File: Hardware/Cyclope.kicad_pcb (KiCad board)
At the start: 2 copper layers, 100 x 84 mm, 81 parts, among them J1 M20-9762042, J2 Motor_2, J3 Motor_1, J4 Front, J5 Front, J8 FTDI, M1 FS5113R, M2 FS5113R, Q1 DMG3414U, Q2 DMG2301L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

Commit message: (Hardware] Renamed motherboard PCB mounting holes for more coherency.
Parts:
- H10, H7, H8, H9: value Raspberry_Pi -> Motherboard
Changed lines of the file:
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@@
       (effects (font (size 1 1) (thickness 0.15)))
     )
-    (fp_text value Raspberry_Pi (at 0 4.2) (layer F.Fab) hide
+    (fp_text value Motherboard (at 0 4.2) (layer F.Fab) hide
       (effects (font (size 1 1) (thickness 0.15)))
     )
@@
       (effects (font (size 1 1) (thickness 0.15)))
     )
-    (fp_text value Raspberry_Pi (at 0 4.2) (layer F.Fab) hide
+    (fp_text value Motherboard (at 0 4.2) (layer F.Fab) hide
       (effects (font (size 1 1) (thickness 0.15)))
     )
@@
       (effects (font (size 1 1) (thickness 0.15)))
     )
-    (fp_text value Raspberry_Pi (at 0 4.2) (layer F.Fab) hide
+    (fp_text value Motherboard (at 0 4.2) (layer F.Fab) hide
       (effects (font (size 1 1) (thickness 0.15)))
     )
@@
       (effects (font (size 1 1) (thickness 0.15)))
     )
-    (fp_text value Raspberry_Pi (at 0 4.2) (layer F.Fab) hide
+    (fp_text value Motherboard (at 0 4.2) (layer F.Fab) hide
       (effects (font (size 1 1) (thickness 0.15)))
     )

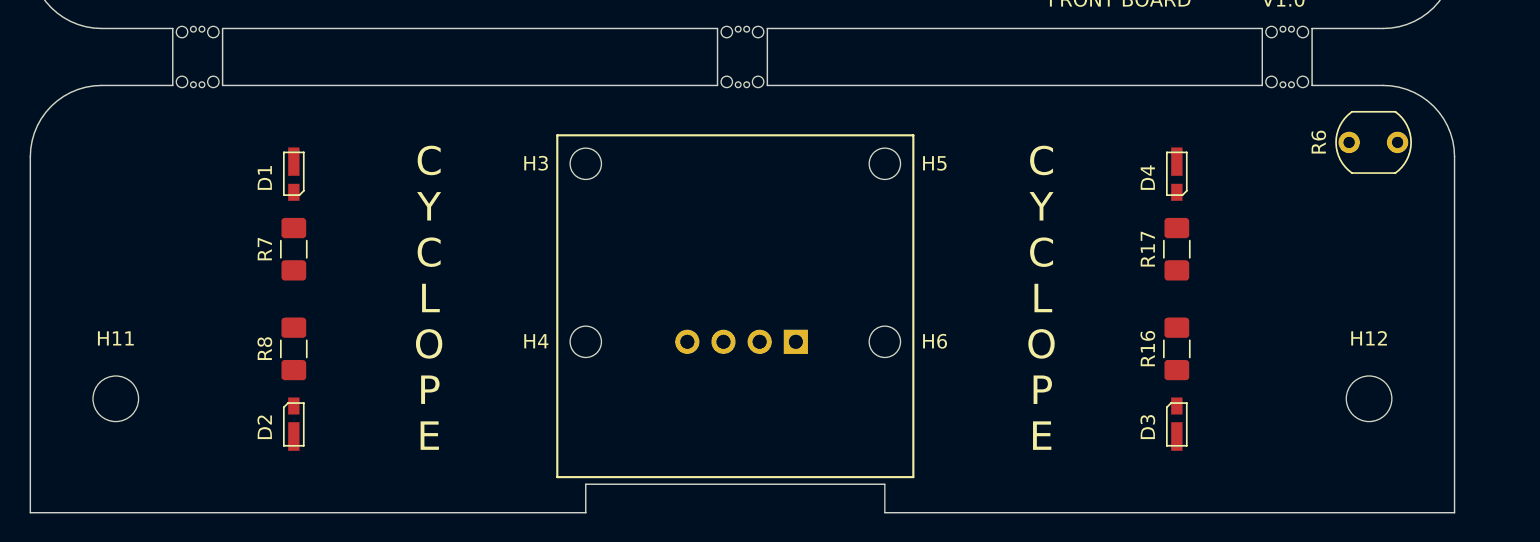
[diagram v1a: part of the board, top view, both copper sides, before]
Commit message: [Hardware] Routed front board PCB.
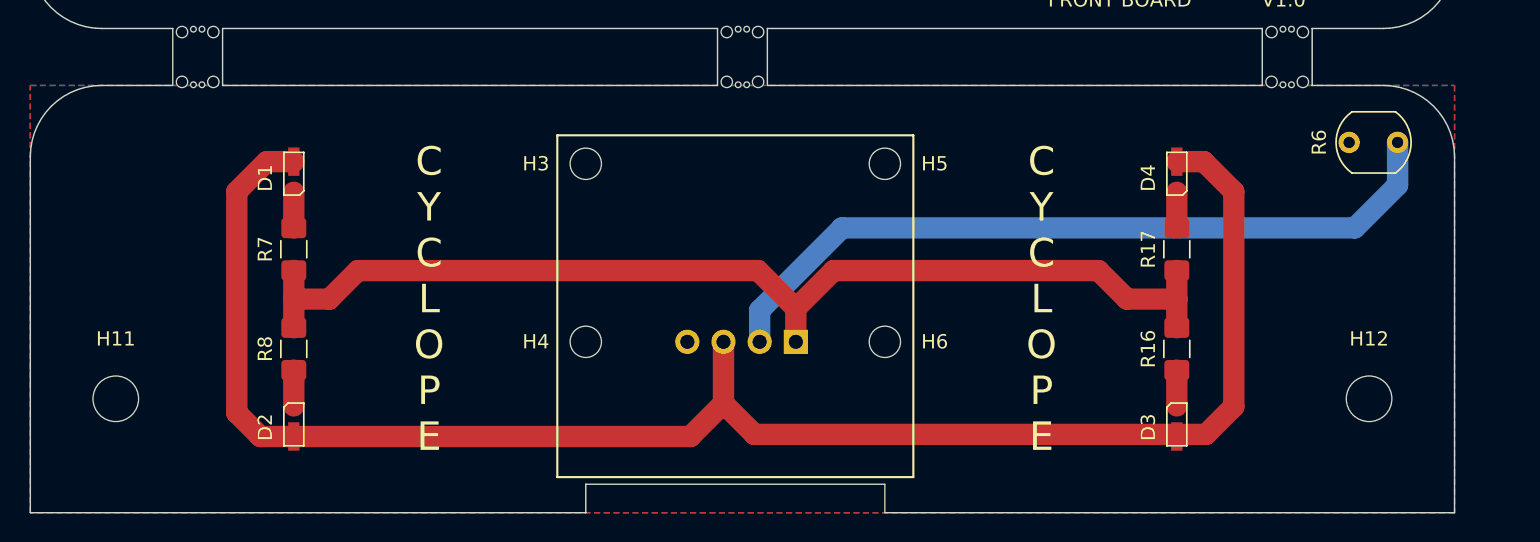
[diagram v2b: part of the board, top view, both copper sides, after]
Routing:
- net Net-(D1-Pad1): track 0.00 -> 118.1 mm
- net +5VD: track 0.00 -> 76.3 mm
- net Net-(J4-Pad2): track 0.00 -> 53.6 mm
- net Net-(D4-Pad2): track 0.00 -> 2.51 mm
- net Net-(D1-Pad2): track 0.00 -> 2.51 mm
- net Net-(D3-Pad2): track 0.00 -> 2.51 mm
- net Net-(D2-Pad2): track 0.00 -> 2.51 mm
- added copper zone on B.Cu, net GNDD
- added copper zone on F.Cu, net GNDD
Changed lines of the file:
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@@
     (thickness 1.6)
     (drawings 64)
-    (tracks 0)
+    (tracks 36)
     (zones 0)
     (modules 81)
@@
   )
   (setup
-    (last_trace_width 0.25)
+    (last_trace_width 1.5)
+    (user_trace_width 1.5)
     (trace_clearance 0.2)
-    (zone_clearance 0.508)
+    (zone_clearance 0.127)
     (zone_45_only no)
     (trace_min 0.2)
@@
     (effects (font (size 1 1) (thickness 0.15)))
   )
+  (segment (start 74.1 119.35) (end 72 121.45) (width 1.5) (layer F.Cu) (net 42))
+  (segment (start 76 119.35) (end 74.1 119.35) (width 1.5) (layer F.Cu) (net 42))
+  (segment (start 72 121.45) (end 72 137) (width 1.5) (layer F.Cu) (net 42))
+  (segment (start 73.65 138.65) (end 76 138.65) (width 1.5) (layer F.Cu) (net 42))
+  (segment (start 72 137) (end 73.65 138.65) (width 1.5) (layer F.Cu) (net 42))
+  (segment (start 76 138.65) (end 103.85 138.65) (width 1.5) (layer F.Cu) (net 42))
+  (segment (start 106.17 136.33) (end 106.17 132) (width 1.5) (layer F.Cu) (net 42))
+  (segment (start 103.85 138.65) (end 106.17 136.33) (width 1.5) (layer F.Cu) (net 42))
+  (segment (start 139.9 119.35) (end 142 121.45) (width 1.5) (layer F.Cu) (net 42))
+  (segment (start 138 119.35) (end 139.9 119.35) (width 1.5) (layer F.Cu) (net 42))
+  (segment (start 142 136.55) (end 140.05 138.5) (width 1.5) (layer F.Cu) (net 42))
+  (segment (start 142 121.45) (end 142 136.55) (width 1.5) (layer F.Cu) (net 42))
+  (segment (start 108.34 138.5) (end 106.17 136.33) (width 1.5) (layer F.Cu) (net 42))
+  (segment (start 140.05 138.5) (end 108.34 138.5) (width 1.5) (layer F.Cu) (net 42))
+  (segment (start 76 121.5) (end 76 124.0125) (width 1.5) (layer F.Cu) (net 43))
+  (segment (start 76 133.9875) (end 76 136.5) (width 1.5) (layer F.Cu) (net 44))
+  (segment (start 111.25 129.65) (end 113.9 127) (width 1.5) (layer F.Cu) (net 46))
+  (segment (start 111.25 132) (end 111.25 129.65) (width 1.5) (layer F.Cu) (net 46))
+  (segment (start 113.9 127) (end 132.5 127) (width 1.5) (layer F.Cu) (net 46))
+  (segment (start 138 129) (end 134.5 129) (width 1.5) (layer F.Cu) (net 46))
+  (segment (start 134.5 129) (end 132.5 127) (width 1.5) (layer F.Cu) (net 46))
+  (segment (start 138 126.9875) (end 138 129) (width 1.5) (layer F.Cu) (net 46))
+  (segment (start 138 129) (end 138 131.0125) (width 1.5) (layer F.Cu) (net 46))
+  (segment (start 76 126.9875) (end 76 129) (width 1.5) (layer F.Cu) (net 46))
+  (segment (start 76 129) (end 76 131.0125) (width 1.5) (layer F.Cu) (net 46))
+  (segment (start 108.6 127) (end 111.25 129.65) (width 1.5) (layer F.Cu) (net 46))
+  (segment (start 80.5 127) (end 108.6 127) (width 1.5) (layer F.Cu) (net 46))
+  (segment (start 78.5 129) (end 80.5 127) (width 1.5) (layer F.Cu) (net 46))
+  (segment (start 76 129) (end 78.5 129) (width 1.5) (layer F.Cu) (net 46))
+  (segment (start 138 133.9875) (end 138 136.5) (width 1.5) (layer F.Cu) (net 56))
+  (segment (start 138 121.5) (end 138 124.0125) (width 1.5) (layer F.Cu) (net 57))
+  (segment (start 153.5 121) (end 153.5 118) (width 1.5) (layer B.Cu) (net 59))
+  (segment (start 114.5 124) (end 150.5 124) (width 1.5) (layer B.Cu) (net 59))
+  (segment (start 108.71 129.79) (end 114.5 124) (width 1.5) (layer B.Cu) (net 59))
+  (segment (start 150.5 124) (end 153.5 121) (width 1.5) (layer B.Cu) (net 59))
+  (segment (start 108.71 132) (end 108.71 129.79) (width 1.5) (layer B.Cu) (net 59))
   (zone (net 0) (net_name "") (layers F&B.Cu) (hatch edge 0.508)
     (connect_pads (clearance 0.508))
@@
       )
     )
+  )
+  (zone (net 45) (net_name GNDD) (layer F.Cu) (hatch edge 0.508)
+    (connect_pads (clearance 0.127))
+    (min_thickness 0.254)
+    (fill yes (arc_segments 32) (thermal_gap 0.508) (thermal_bridge_width 0.508))
+    (polygon
+      (pts
+        (xy 157.5 144) (xy 57.5 144) (xy 57.5 114) (xy 157.5 114)
+      )
+    )
+  )
+  (zone (net 45) (net_name GNDD) (layer B.Cu) (hatch edge 0.508)
+    (connect_pads (clearance 0.127))
+    (min_thickness 0.254)
+    (fill yes (arc_segments 32) (thermal_gap 0.508) (thermal_bridge_width 0.508))
+    (polygon
+      (pts
+        (xy 157.5 144) (xy 57.5 144) (xy 57.5 114) (xy 157.5 114)
+      )
+    )

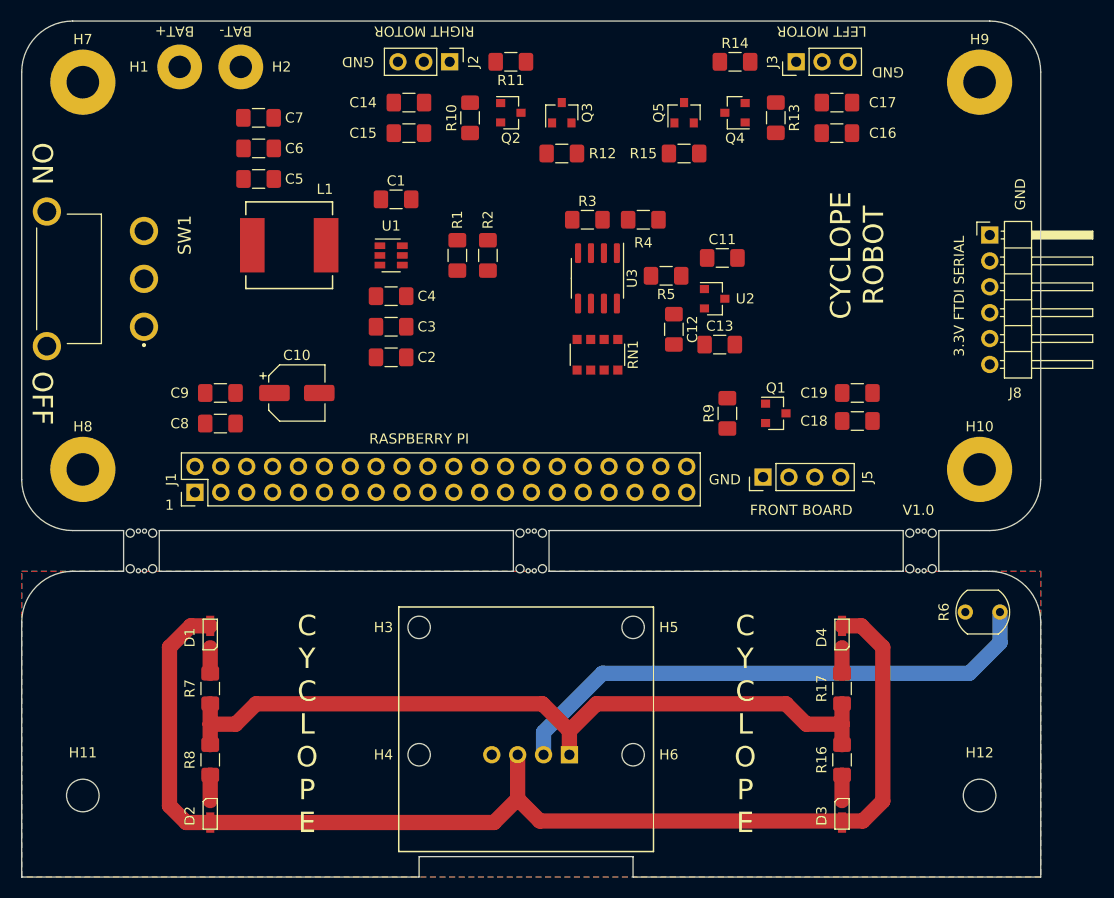
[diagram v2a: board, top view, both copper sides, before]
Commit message: [Hardware] Routed motherboard left motor transistors.
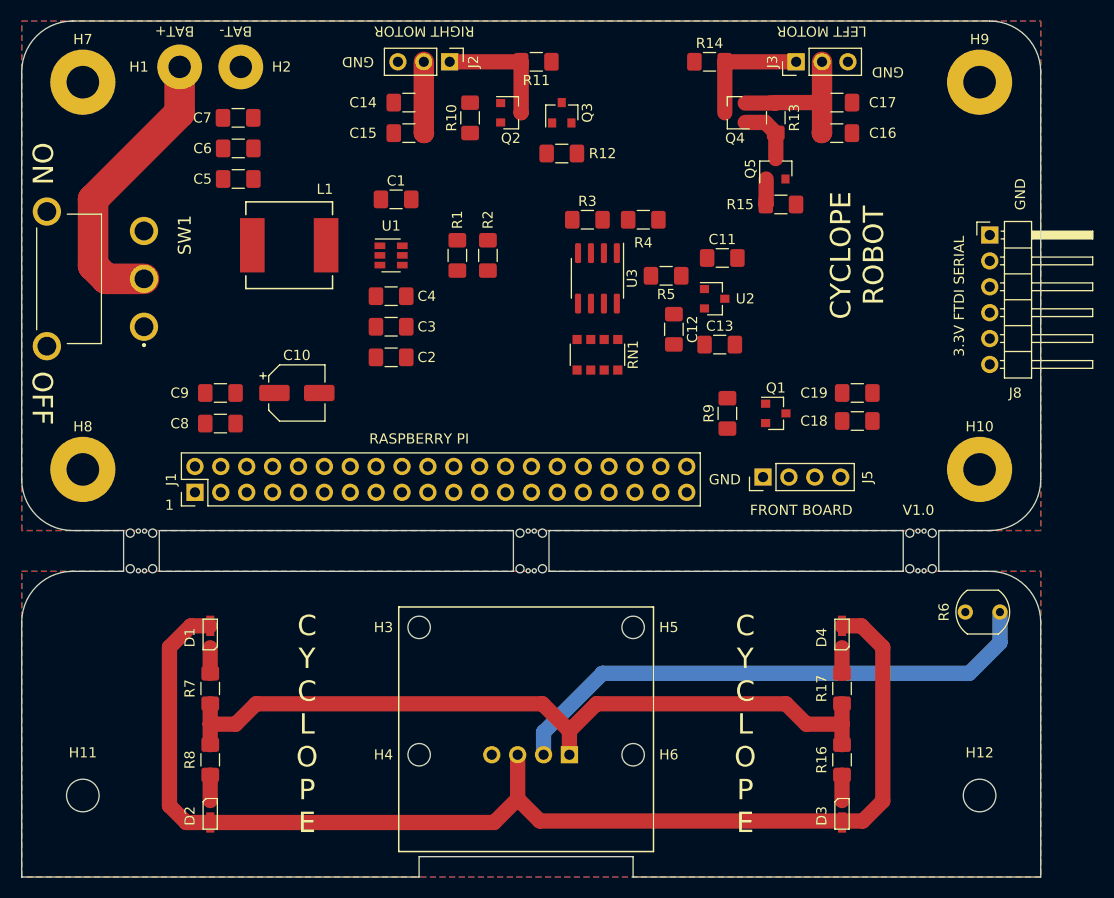
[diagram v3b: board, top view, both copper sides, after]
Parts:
- moved R15 10.7 mm to (132.0, 78.0)
- moved Q5 10.5 mm to (131.5, 74.5)
- moved R11 2.50 mm to (108.0, 64.0)
- moved R14 2.50 mm to (125.0, 64.0)
- moved C5 2.00 mm to (78.8, 75.5), turned to 0 degrees
- moved C6 2.00 mm to (78.8, 72.5), turned to 0 degrees
- moved C7 2.00 mm to (78.7, 69.5), turned to 0 degrees
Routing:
- net Net-(H1-Pad1): track 0.00 -> 28.6 mm
- net +5V: track 0.00 -> 21.6 mm
- net Net-(J3-Pad1): track 0.00 -> 12.0 mm
- net Net-(J2-Pad1): track 0.00 -> 12.0 mm
- net Net-(Q4-Pad1): track 0.00 -> 5.95 mm
- net Net-(J1-Pad32): track 0.00 -> 2.52 mm
- added copper zone on B.Cu, net GND
- added copper zone on F.Cu, net GND

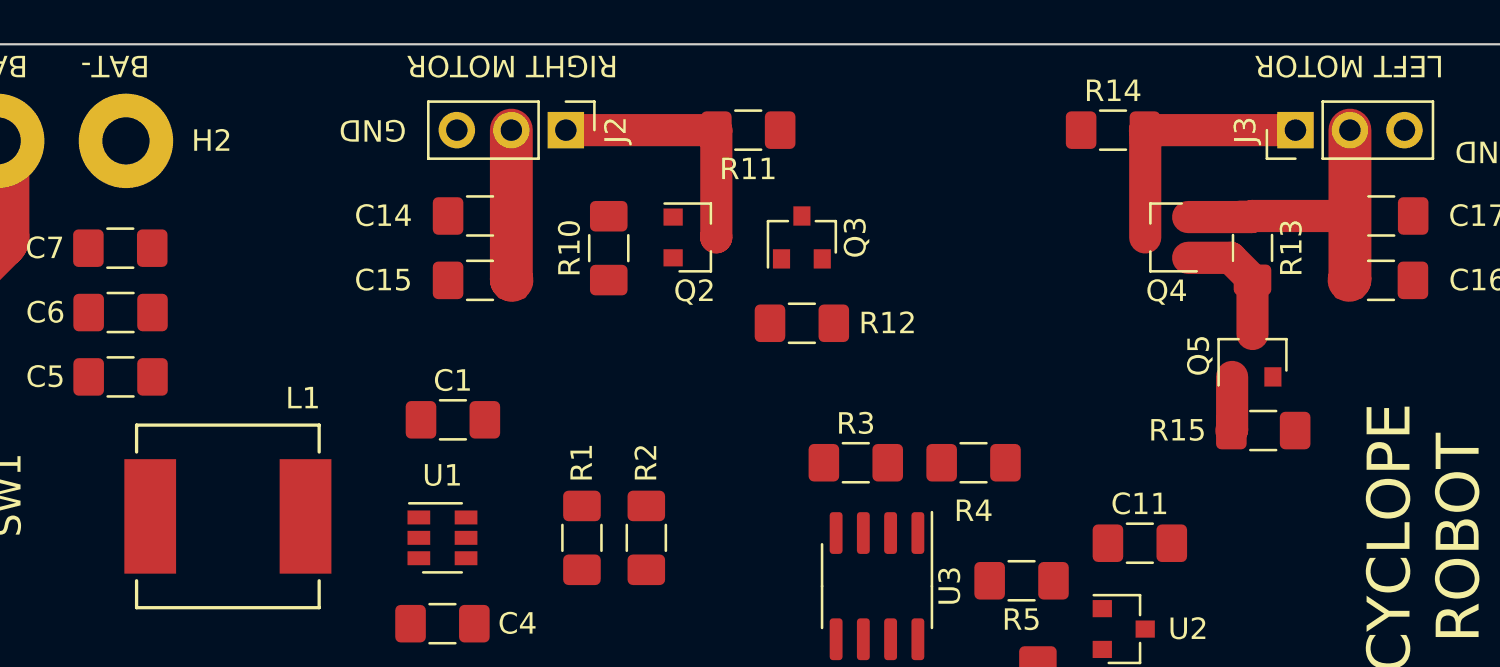
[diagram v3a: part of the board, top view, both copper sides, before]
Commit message: [Hardware] Routed motherboard right motor transistors.
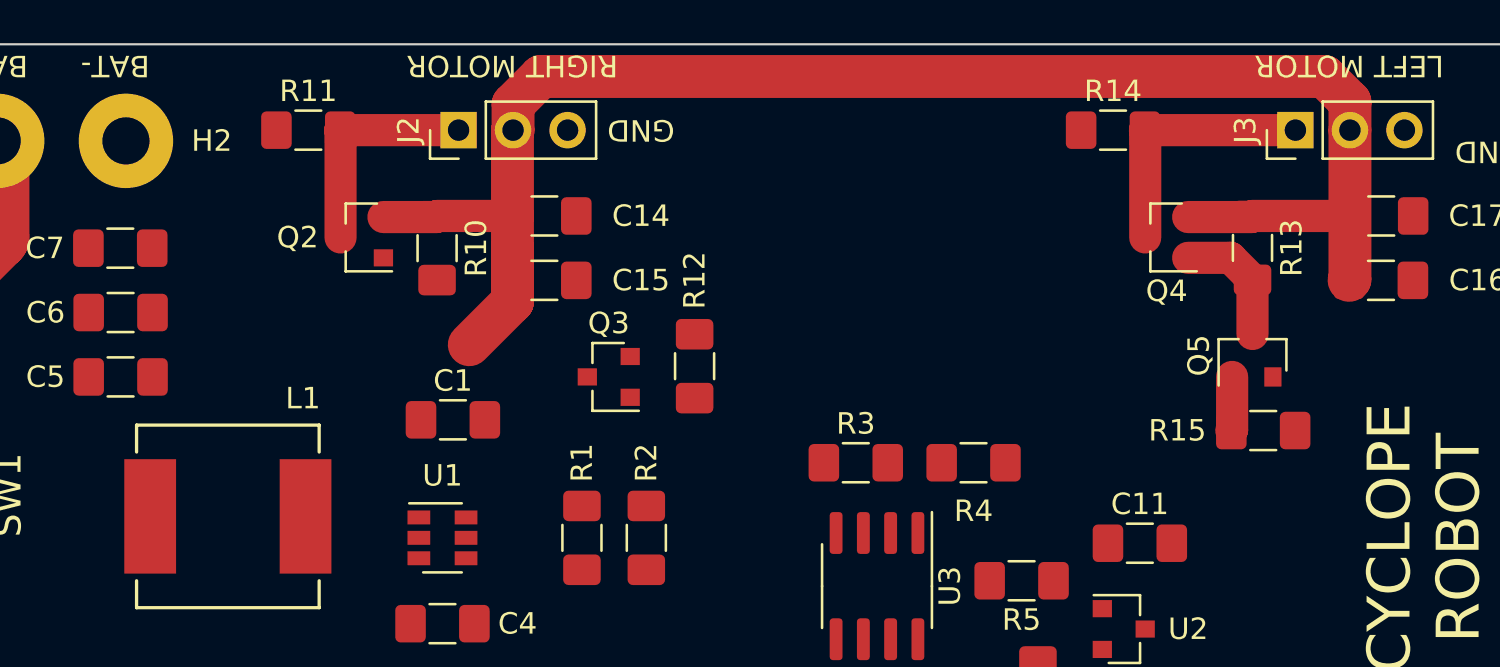
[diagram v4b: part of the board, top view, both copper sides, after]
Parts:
- moved R11 20.5 mm to (87.5, 64.0), turned to 0 degrees
- moved Q2 15.5 mm to (90.0, 69.0), turned to 180 degrees
- moved Q3 11.1 mm to (101.5, 75.5), turned to 180 degrees
- moved R10 8.00 mm to (93.5, 69.5), turned to 270 degrees
- moved R12 5.39 mm to (105.5, 75.0), turned to 90 degrees
- moved J2 5.00 mm to (94.5, 64.0), turned to 90 degrees
- moved C14 3.00 mm to (98.5, 68.0), turned to 180 degrees
- moved C15 3.00 mm to (98.5, 71.0), turned to 180 degrees
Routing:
- net +5V: track 21.6 -> 76.6 mm
- net Net-(J2-Pad1): track 12.0 -> 10.5 mm
